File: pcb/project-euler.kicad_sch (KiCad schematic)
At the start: 4 parts

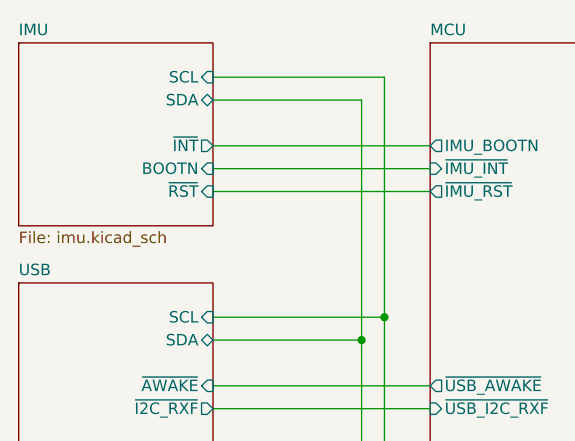
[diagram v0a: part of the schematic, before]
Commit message: [firmware/pcb] Initial firmware upload + fixed mistake in PCB + added errata documentation
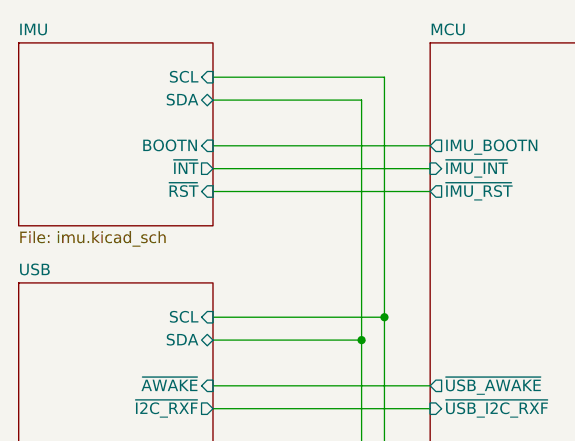
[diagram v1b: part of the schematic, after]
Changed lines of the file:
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@@
+	(wire
+		(pts
+			(xy 151.13 67.31) (xy 153.67 67.31)
+		)
+		(stroke
+			(width 0)
+			(type default)
+		)
+	)
+	(wire
+		(pts
+			(xy 59.69 85.09) (xy 83.82 85.09)
+		)
+		(stroke
+			(width 0)
+			(type default)
+		)
+	)
+	(wire
+		(pts
+			(xy 59.69 90.17) (xy 83.82 90.17)
+		)
+		(stroke
+			(width 0)
+			(type default)
+		)
+	)
+	(wire
+		(pts
+			(xy 151.13 58.42) (xy 153.67 58.42)
+		)
+		(stroke
+			(width 0)
+			(type default)
+		)
+	)
+	(wire
+		(pts
+			(xy 78.74 74.93) (xy 78.74 48.26)
+		)
+		(stroke
+			(width 0)
+			(type default)
+		)
+	)
+	(wire
+		(pts
+			(xy 59.69 50.8) (xy 76.2 50.8)
+		)
+		(stroke
+			(width 0)
+			(type default)
+		)
+	)
+	(wire
+		(pts
+			(xy 151.13 49.53) (xy 153.67 49.53)
+		)
+		(stroke
+			(width 0)
+			(type default)
+		)
+	)
 	(wire
 		(pts
@@
 	(wire
 		(pts
-			(xy 151.13 67.31) (xy 153.67 67.31)
-		)
-		(stroke
-			(width 0)
-			(type default)
-		)
-	)
-	(wire
-		(pts
-			(xy 59.69 85.09) (xy 83.82 85.09)
-		)
-		(stroke
-			(width 0)
-			(type default)
-		)
-	)
-	(wire
-		(pts
-			(xy 59.69 90.17) (xy 83.82 90.17)
-		)
-		(stroke
-			(width 0)
-			(type default)
-		)
-	)
-	(wire
-		(pts
-			(xy 151.13 58.42) (xy 153.67 58.42)
-		)
-		(stroke
-			(width 0)
-			(type default)
-		)
-	)
-	(wire
-		(pts
-			(xy 78.74 74.93) (xy 78.74 48.26)
-		)
-		(stroke
-			(width 0)
-			(type default)
-		)
-	)
-	(wire
-		(pts
-			(xy 59.69 50.8) (xy 76.2 50.8)
-		)
-		(stroke
-			(width 0)
-			(type default)
-		)
-	)
-	(wire
-		(pts
-			(xy 151.13 49.53) (xy 153.67 49.53)
-		)
-		(stroke
-			(width 0)
-			(type default)
-		)
-	)
-	(wire
-		(pts
 			(xy 59.69 82.55) (xy 83.82 82.55)
 		)
@@
 	(wire
 		(pts
+			(xy 59.69 31.75) (xy 83.82 31.75)
+		)
+		(stroke
+			(width 0)
+			(type default)
+		)
+	)
+	(wire
+		(pts
 			(xy 59.69 55.88) (xy 83.82 55.88)
 		)
@@
 		(pts
 			(xy 153.67 58.42) (xy 153.67 49.53)
-		)
-		(stroke
-			(width 0)
-			(type default)
-		)
-	)
-	(wire
-		(pts
-			(xy 59.69 31.75) (xy 83.82 31.75)
 		)
 		(stroke
@@
 		)
 		(instances
-			(project "head-tracker"
+			(project "project-euler"
 				(path "/e3362552-3508-4d8c-a74b-6e4b5fd45312"
 					(page "2")
@@
 		)
 		(instances
-			(project "head-tracker"
+			(project "project-euler"
 				(path "/e3362552-3508-4d8c-a74b-6e4b5fd45312"
 					(page "3")
@@
 		)
 		(instances
-			(project "head-tracker"
+			(project "project-euler"
 				(path "/e3362552-3508-4d8c-a74b-6e4b5fd45312"
 					(page "4")
@@
 		)
 		(pin "BOOTN" input
+			(at 59.69 29.21 0)
+			(effects
+				(font
+					(size 1.27 1.27)
+				)
+				(justify right)
+			)
+		)
+		(pin "~{INT}" output
 			(at 59.69 31.75 0)
-			(effects
-				(font
-					(size 1.27 1.27)
-				)
-				(justify right)
-			)
-		)
-		(pin "~{INT}" output
-			(at 59.69 29.21 0)
 			(effects
 				(font
@@
 		)
 		(instances
-			(project "head-tracker"
+			(project "project-euler"
 				(path "/e3362552-3508-4d8c-a74b-6e4b5fd45312"
 					(page "5")
